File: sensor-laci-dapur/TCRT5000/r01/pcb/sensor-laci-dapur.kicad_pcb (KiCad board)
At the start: 2 copper layers, 66 x 14 mm, 8 parts

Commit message: Sensor Laci Dapur TCRT5000L rev01b
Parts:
- removed Port: Out GND +5, Connectors_Molex:Molex_KK-6410-03_03x2.54mm_Straight
- removed the REF** at (142.2, 95.2)
- removed the REF** at (161.3, 95.2)
- removed Sensor: TCRT5000L, TCRT5000L:XDCR_TCRT5000L
- added M: 1pin, Connect:1pin, F.Cu at (138.2, 97.8)
- added Port1: 1_Out, Connectors_Molex:Molex_KK-6410-03_03x2.54mm_Straight, F.Cu at (177.8, 95.2)
- added REF**: 1pin, Connect:1pin, F.Cu at (164.1, 97.8)
- added Sensor1: TCRT5000L, TCRT5000L:XDCR_TCRT5000L, F.Cu at (151.1, 97.8)
- moved REF** 43.3 mm to (126.5, 97.3)
- moved R1 14.2 mm to (121.9, 105.7), turned to 90 degrees
- moved R2 11.4 mm to (126.5, 105.7), turned to 90 degrees
- moved R3 9.18 mm to (130.8, 105.7), turned to 90 degrees
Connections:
- R1 pad 2: Net-(Port1-Pad2) -> /GND
- R2 pad 1: Net-(Port1-Pad3) -> /Out
- R3 pad 1: Net-(Port1-Pad1) -> /+5V
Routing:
- net Net-(Port1-Pad3): track 62.0 -> 0.00 mm
- net /Out: track 0.00 -> 53.9 mm
- net Net-(Port1-Pad1): track 49.0 -> 0.00 mm
- net Net-(R3-Pad2): track 45.3 -> 27.3 mm
- net Net-(R1-Pad1): track 34.6 -> 42.4 mm
- added copper zone on B.Cu, net /+5V
- added copper zone on F.Cu, net /GND
- removed copper zone on B.Cu, net Net-(Port1-Pad2)
- removed copper zone on F.Cu, net Net-(Port1-Pad2)
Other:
- board size 66 x 14 mm -> 68.6 x 22.9 mm
- net class +5 removed
- net class Default: clearance 0.2 -> 0.3; trace_width 0.25 -> 0.4
- net class Signal added: clearance 0.3, trace_width 0.4, via_dia 0.6, via_drill 0.4
- rule trace_clearance: 0.2 -> 0.3
- board text added: "Out GND +5V"
- board text added: "TCRT500L"
- board text added: "rev01"

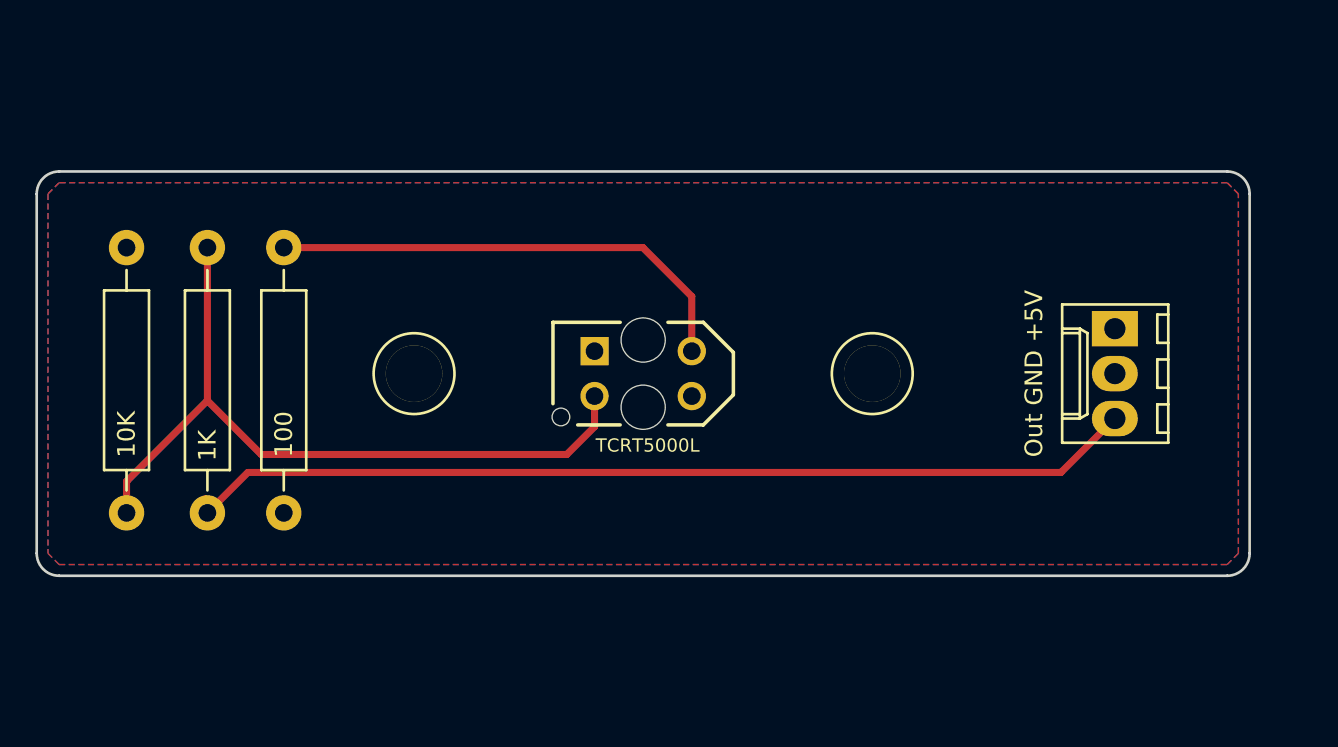
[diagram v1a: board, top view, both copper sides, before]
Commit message: Change connector to JST-XH Angled
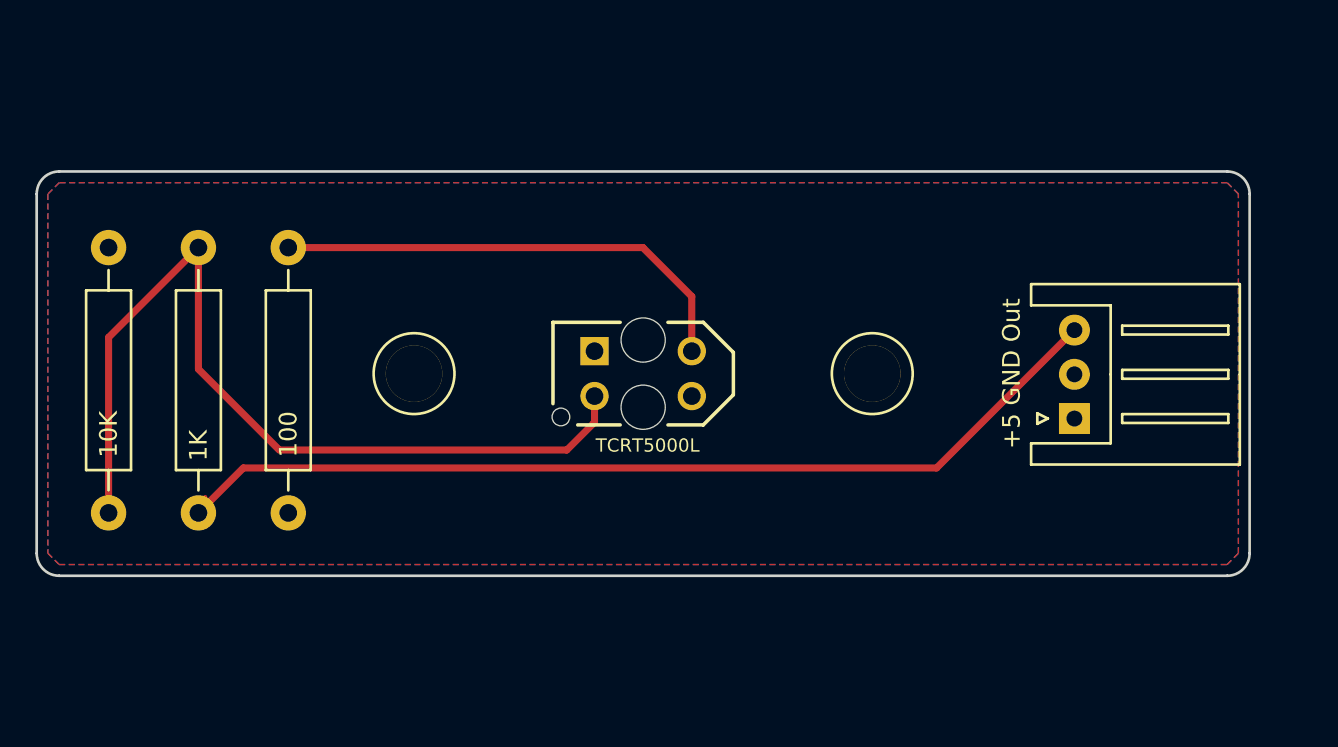
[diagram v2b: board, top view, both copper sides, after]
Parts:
- Port1: footprint Connectors_Molex:Molex_KK-6410-03_03x2.54mm_Straight -> Connectors_JST:JST_XH_S03B-XH-A_03x2.50mm_Angled
- moved Port1 5.57 mm to (175.5, 100.3), turned to 90 degrees
- moved R1 1.02 mm to (120.9, 105.7)
- moved R2 0.51 mm to (126.0, 105.7)
- moved R3 0.25 mm to (131.1, 105.7)
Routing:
- net Net-(R1-Pad1): track 42.4 -> 50.4 mm
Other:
- board text added: "+5 GND Out"
- board text removed: "Out GND +5V"
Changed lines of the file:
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@@
     (40 Dwgs.User user)
     (41 Cmts.User user)
-    (42 Eco1.User user hide)
+    (42 Eco1.User user)
     (43 Eco2.User user)
     (44 Edge.Cuts user)
@@
   )
   (module Resistors_ThroughHole:Resistor_Horizontal_RM15mm (layer F.Cu)
-    (at 126.492 105.664 90)
+    (at 125.984 105.664 90)
     (descr "Resistor, Axial, RM 15mm,")
     (tags "Resistor Axial RM 15mm")
@@
     )
   )
-  (module Connectors_Molex:Molex_KK-6410-03_03x2.54mm_Straight (layer F.Cu)
-    (at 177.8 95.25 270)
-    (descr "Connector Headers with Friction Lock, 22-27-2031, http://www.molex.com/pdm_docs/sd/022272021_sd.pdf")
-    (tags "connector molex kk_6410 22-27-2031")
-    (fp_text reference Port1 (at 1 -4.5 270) (layer F.SilkS) hide
-      (effects (font (size 1 1) (thickness 0.15)))
-    )
-    (fp_text value 1_Out (at 2.54 4.5 270) (layer F.Fab) hide
-      (effects (font (size 1 1) (thickness 0.15)))
-    )
-    (fp_line (start -1.37 -3.02) (end -1.37 2.98) (layer F.SilkS) (width 0.15))
-    (fp_line (start -1.37 2.98) (end 6.45 2.98) (layer F.SilkS) (width 0.15))
-    (fp_line (start 6.45 2.98) (end 6.45 -3.02) (layer F.SilkS) (width 0.15))
-    (fp_line (start 6.45 -3.02) (end -1.37 -3.02) (layer F.SilkS) (width 0.15))
-    (fp_line (start 0 2.98) (end 0 1.98) (layer F.SilkS) (width 0.15))
-    (fp_line (start 0 1.98) (end 5.08 1.98) (layer F.SilkS) (width 0.15))
-    (fp_line (start 5.08 1.98) (end 5.08 2.98) (layer F.SilkS) (width 0.15))
-    (fp_line (start 0 1.98) (end 0.25 1.55) (layer F.SilkS) (width 0.15))
-    (fp_line (start 0.25 1.55) (end 4.83 1.55) (layer F.SilkS) (width 0.15))
-    (fp_line (start 4.83 1.55) (end 5.08 1.98) (layer F.SilkS) (width 0.15))
-    (fp_line (start 0.25 2.98) (end 0.25 1.98) (layer F.SilkS) (width 0.15))
-    (fp_line (start 4.83 2.98) (end 4.83 1.98) (layer F.SilkS) (width 0.15))
-    (fp_line (start -0.8 -3.02) (end -0.8 -2.4) (layer F.SilkS) (width 0.15))
-    (fp_line (start -0.8 -2.4) (end 0.8 -2.4) (layer F.SilkS) (width 0.15))
-    (fp_line (start 0.8 -2.4) (end 0.8 -3.02) (layer F.SilkS) (width 0.15))
-    (fp_line (start 1.74 -3.02) (end 1.74 -2.4) (layer F.SilkS) (width 0.15))
-    (fp_line (start 1.74 -2.4) (end 3.34 -2.4) (layer F.SilkS) (width 0.15))
-    (fp_line (start 3.34 -2.4) (end 3.34 -3.02) (layer F.SilkS) (width 0.15))
-    (fp_line (start 4.28 -3.02) (end 4.28 -2.4) (layer F.SilkS) (width 0.15))
-    (fp_line (start 4.28 -2.4) (end 5.88 -2.4) (layer F.SilkS) (width 0.15))
-    (fp_line (start 5.88 -2.4) (end 5.88 -3.02) (layer F.SilkS) (width 0.15))
-    (fp_line (start -1.9 3.5) (end -1.9 -3.55) (layer F.CrtYd) (width 0.05))
-    (fp_line (start -1.9 -3.55) (end 7 -3.55) (layer F.CrtYd) (width 0.05))
-    (fp_line (start 7 -3.55) (end 7 3.5) (layer F.CrtYd) (width 0.05))
-    (fp_line (start 7 3.5) (end -1.9 3.5) (layer F.CrtYd) (width 0.05))
-    (pad 1 thru_hole rect (at 0 0 270) (size 2 2.6) (drill 1.2) (layers *.Cu *.Mask F.SilkS)
-      (net 3 /+5V))
-    (pad 2 thru_hole oval (at 2.54 0 270) (size 2 2.6) (drill 1.2) (layers *.Cu *.Mask F.SilkS)
-      (net 4 /GND))
-    (pad 3 thru_hole oval (at 5.08 0 270) (size 2 2.6) (drill 1.2) (layers *.Cu *.Mask F.SilkS)
-      (net 5 /Out))
-  )
   (module Resistors_ThroughHole:Resistor_Horizontal_RM15mm (layer F.Cu)
-    (at 121.92 105.664 90)
+    (at 120.904 105.664 90)
     (descr "Resistor, Axial, RM 15mm,")
     (tags "Resistor Axial RM 15mm")
@@
   )
   (module Resistors_ThroughHole:Resistor_Horizontal_RM15mm (layer F.Cu)
-    (at 130.81 105.664 90)
+    (at 131.064 105.664 90)
     (descr "Resistor, Axial, RM 15mm,")
     (tags "Resistor Axial RM 15mm")
@@
     (fp_line (start 0.35052 -0.89916) (end 0.7493 -1.89992) (layer B.SilkS) (width 0.15))
   )
+  (module Connectors_JST:JST_XH_S03B-XH-A_03x2.50mm_Angled (layer F.Cu)
+    (at 175.514 100.33 90)
+    (descr "JST XH series connector, S03B-XH-A, side entry type, through hole")
+    (tags "connector jst xh tht side horizontal angled 2.50mm")
+    (fp_text reference Port1 (at 2.54 -3.81 90) (layer F.SilkS) hide
+      (effects (font (size 1 1) (thickness 0.15)))
+    )
+    (fp_text value 1_Out (at 2.5 10.3 90) (layer F.Fab) hide
+      (effects (font (size 1 1) (thickness 0.15)))
+    )
+    (fp_line (start -2.95 -2.8) (end -2.95 9.7) (layer F.CrtYd) (width 0.05))
+    (fp_line (start -2.95 9.7) (end 7.95 9.7) (layer F.CrtYd) (width 0.05))
+    (fp_line (start 7.95 9.7) (end 7.95 -2.8) (layer F.CrtYd) (width 0.05))
+    (fp_line (start 7.95 -2.8) (end -2.95 -2.8) (layer F.CrtYd) (width 0.05))
+    (fp_line (start 2.5 9.35) (end -2.6 9.35) (layer F.SilkS) (width 0.15))
+    (fp_line (start -2.6 9.35) (end -2.6 -2.45) (layer F.SilkS) (width 0.15))
+    (fp_line (start -2.6 -2.45) (end -1.4 -2.45) (layer F.SilkS) (width 0.15))
+    (fp_line (start -1.4 -2.45) (end -1.4 2.05) (layer F.SilkS) (width 0.15))
+    (fp_line (start -1.4 2.05) (end 2.5 2.05) (layer F.SilkS) (width 0.15))
+    (fp_line (start 2.5 9.35) (end 7.6 9.35) (layer F.SilkS) (width 0.15))
+    (fp_line (start 7.6 9.35) (end 7.6 -2.45) (layer F.SilkS) (width 0.15))
+    (fp_line (start 7.6 -2.45) (end 6.4 -2.45) (layer F.SilkS) (width 0.15))
+    (fp_line (start 6.4 -2.45) (end 6.4 2.05) (layer F.SilkS) (width 0.15))
+    (fp_line (start 6.4 2.05) (end 2.5 2.05) (layer F.SilkS) (width 0.15))
+    (fp_line (start -0.25 2.7) (end -0.25 8.7) (layer F.SilkS) (width 0.15))
+    (fp_line (start -0.25 8.7) (end 0.25 8.7) (layer F.SilkS) (width 0.15))
+    (fp_line (start 0.25 8.7) (end 0.25 2.7) (layer F.SilkS) (width 0.15))
+    (fp_line (start 0.25 2.7) (end -0.25 2.7) (layer F.SilkS) (width 0.15))
+    (fp_line (start 2.25 2.7) (end 2.25 8.7) (layer F.SilkS) (width 0.15))
+    (fp_line (start 2.25 8.7) (end 2.75 8.7) (layer F.SilkS) (width 0.15))
+    (fp_line (start 2.75 8.7) (end 2.75 2.7) (layer F.SilkS) (width 0.15))
+    (fp_line (start 2.75 2.7) (end 2.25 2.7) (layer F.SilkS) (width 0.15))
+    (fp_line (start 4.75 2.7) (end 4.75 8.7) (layer F.SilkS) (width 0.15))
+    (fp_line (start 4.75 8.7) (end 5.25 8.7) (layer F.SilkS) (width 0.15))
+    (fp_line (start 5.25 8.7) (end 5.25 2.7) (layer F.SilkS) (width 0.15))
+    (fp_line (start 5.25 2.7) (end 4.75 2.7) (layer F.SilkS) (width 0.15))
+    (fp_line (start 0 -1.5) (end -0.3 -2.1) (layer F.SilkS) (width 0.15))
+    (fp_line (start -0.3 -2.1) (end 0.3 -2.1) (layer F.SilkS) (width 0.15))
+    (fp_line (start 0.3 -2.1) (end 0 -1.5) (layer F.SilkS) (width 0.15))
+    (pad 1 thru_hole rect (at 0 0 90) (size 1.75 1.75) (drill 0.9) (layers *.Cu *.Mask F.SilkS)
+      (net 3 /+5V))
+    (pad 2 thru_hole circle (at 2.5 0 90) (size 1.75 1.75) (drill 0.9) (layers *.Cu *.Mask F.SilkS)
+      (net 4 /GND))
+    (pad 3 thru_hole circle (at 5 0 90) (size 1.75 1.75) (drill 0.9) (layers *.Cu *.Mask F.SilkS)
+      (net 5 /Out))
+    (model Connectors_JST.3dshapes/JST_XH_S03B-XH-A_03x2.50mm_Angled.wrl
+      (at (xyz 0 0 0))
+      (scale (xyz 1 1 1))
+      (rotate (xyz 0 0 0))
+    )
+  )
   (gr_text TCRT500L (at 183.896 91.694) (layer B.SilkS)
     (effects (font (size 1.5 1.5) (thickness 0.3)) (justify left mirror))
@@
     (effects (font (size 1 1) (thickness 0.2)) (justify left mirror))
   )
-  (gr_text "Out GND +5V" (at 173.228 97.79 90) (layer F.SilkS)
+  (gr_text "+5 GND Out" (at 171.958 97.79 90) (layer F.SilkS)
     (effects (font (size 1 1) (thickness 0.15)))
   )
@@
   (gr_line (start 118.11 109.22) (end 184.15 109.22) (angle 90) (layer Edge.Cuts) (width 0.15))
   (gr_line (start 116.84 87.63) (end 116.84 107.95) (angle 90) (layer Edge.Cuts) (width 0.15))
-  (segment (start 121.92 105.664) (end 121.92 103.886) (width 0.4) (layer F.Cu) (net 1))
-  (segment (start 121.92 103.886) (end 126.492 99.314) (width 0.4) (layer F.Cu) (net 1))
-  (segment (start 126.492 90.664) (end 126.492 99.314) (width 0.4) (layer F.Cu) (net 1))
-  (segment (start 148.38 100.794) (end 148.38 99.06) (width 0.4) (layer F.Cu) (net 1))
-  (segment (start 146.812 102.362) (end 148.38 100.794) (width 0.4) (layer F.Cu) (net 1))
-  (segment (start 129.54 102.362) (end 146.812 102.362) (width 0.4) (layer F.Cu) (net 1))
-  (segment (start 126.492 99.314) (end 129.54 102.362) (width 0.4) (layer F.Cu) (net 1))
-  (segment (start 130.81 90.664) (end 151.116 90.664) (width 0.4) (layer F.Cu) (net 2))
+  (segment (start 125.984 97.536) (end 125.984 90.664) (width 0.4) (layer F.Cu) (net 1))
+  (segment (start 130.556 102.108) (end 125.984 97.536) (width 0.4) (layer F.Cu) (net 1))
+  (segment (start 146.812 102.108) (end 130.556 102.108) (width 0.4) (layer F.Cu) (net 1))
+  (segment (start 148.38 100.54) (end 146.812 102.108) (width 0.4) (layer F.Cu) (net 1))
+  (segment (start 148.38 99.06) (end 148.38 100.54) (width 0.4) (layer F.Cu) (net 1))
+  (segment (start 120.904 95.744) (end 125.984 90.664) (width 0.4) (layer F.Cu) (net 1))
+  (segment (start 120.904 105.664) (end 120.904 95.744) (width 0.4) (layer F.Cu) (net 1))
   (segment (start 153.88 93.428) (end 153.88 96.52) (width 0.4) (layer F.Cu) (net 2))
   (segment (start 151.116 90.664) (end 153.88 93.428) (width 0.4) (layer F.Cu) (net 2))
+  (segment (start 131.064 90.664) (end 151.116 90.664) (width 0.4) (layer F.Cu) (net 2))
   (segment (start 130.81 90.664) (end 130.81 90.678) (width 0.4) (layer F.Cu) (net 2))
-  (segment (start 126.492 105.664) (end 128.778 103.378) (width 0.4) (layer F.Cu) (net 5))
-  (segment (start 174.752 103.378) (end 177.8 100.33) (width 0.4) (layer F.Cu) (net 5))
-  (segment (start 128.778 103.378) (end 174.752 103.378) (width 0.4) (layer F.Cu) (net 5))
+  (segment (start 167.72 103.124) (end 175.514 95.33) (width 0.4) (layer F.Cu) (net 5))
+  (segment (start 128.524 103.124) (end 167.72 103.124) (width 0.4) (layer F.Cu) (net 5))
+  (segment (start 125.984 105.664) (end 128.524 103.124) (width 0.4) (layer F.Cu) (net 5))
   (segment (start 126.365 105.17) (end 126.365 104.775) (width 0.25) (layer F.Cu) (net 5))
   (zone (net 4) (net_name /GND) (layer F.Cu) (hatch edge 0.508)

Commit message: Adjust pin order and component locations
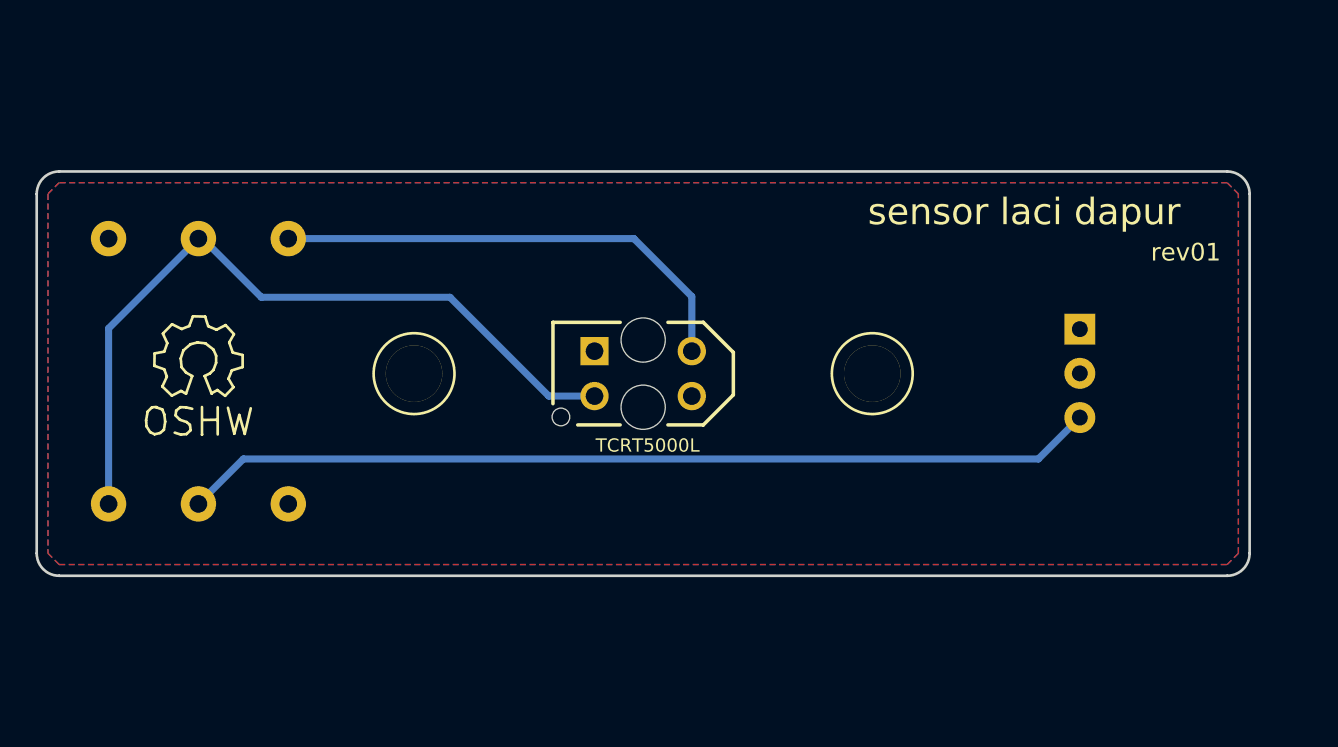
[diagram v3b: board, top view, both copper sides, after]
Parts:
- removed Port1: 1_Out, Connectors_JST:JST_XH_S03B-XH-A_03x2.50mm_Angled
- added U1: 1_Out, Connectors_JST:JST_XH_S03B-XH-A_03x2.50mm_Angled, B.Cu at (175.8, 95.3)
- R1, R2, R3: moved to B.Cu
- REF**: moved to F.Cu
- moved REF** 0.57 mm to (126.0, 97.0), turned to 0 degrees
- moved R1 0.51 mm to (120.9, 105.2)
- moved R2 0.51 mm to (126.0, 105.2)
- moved R3 0.51 mm to (131.1, 105.2)
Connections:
- R1 pad 2: /GND -> /+5V
- R3 pad 1: /+5V -> /GND
- Sensor1 pad 1: /+5V -> /GND
- Sensor1 pad 3: /GND -> /+5V
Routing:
- net Net-(R1-Pad1): track 50.4 -> 43.2 mm
- net /Out: track 54.2 -> 52.3 mm
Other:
- board text added: "GND +5 Out"
- board text removed: "+5 GND Out"
- board text removed: "TCRT500L"

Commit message: Add SMD resistor pad to the sensor board
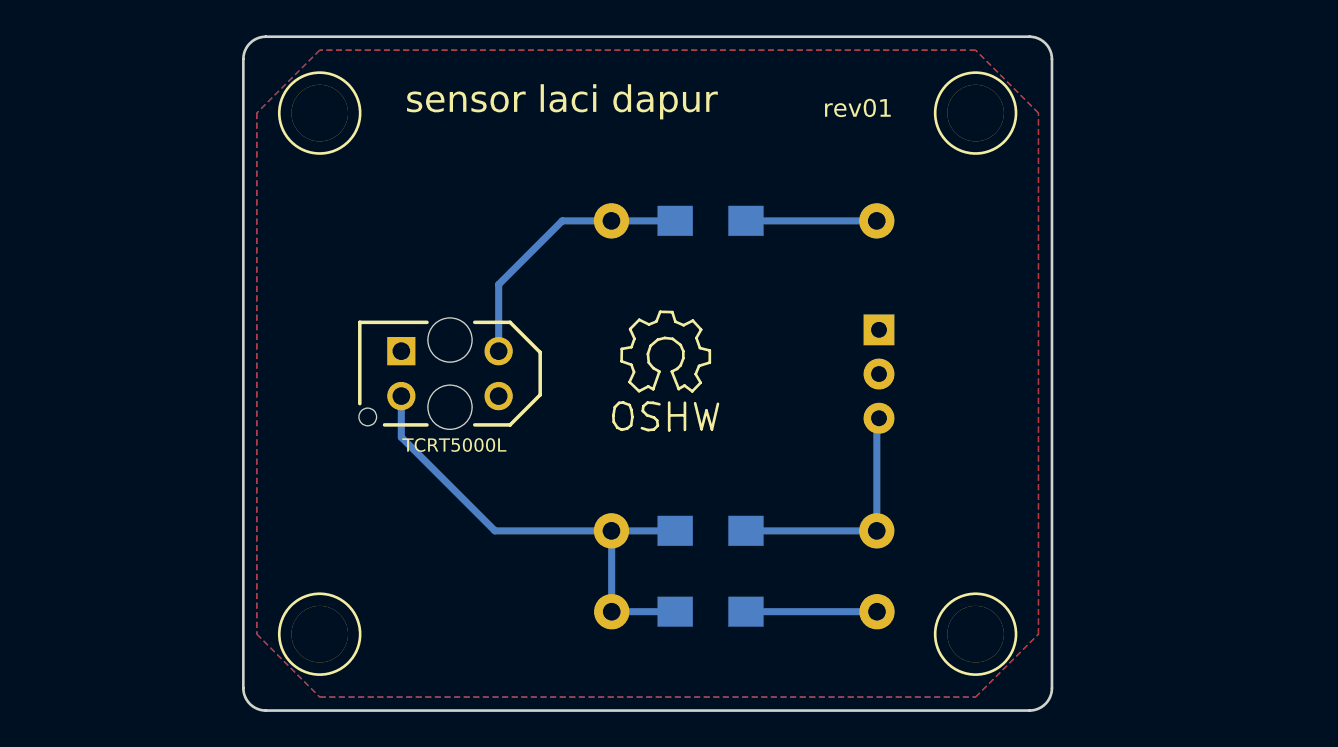
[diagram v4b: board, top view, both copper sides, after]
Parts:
- added R100: R_1206_HandSoldering, Resistors_SMD:R_1206_HandSoldering, B.Cu at (154.9, 89.2)
- added R10K: R_1206_HandSoldering, Resistors_SMD:R_1206_HandSoldering, B.Cu at (154.9, 111.3)
- added R1K: R_1206_HandSoldering, Resistors_SMD:R_1206_HandSoldering, B.Cu at (154.9, 106.7)
- added REF**: 1pin, Connect:1pin, F.Cu at (132.8, 112.5)
- added REF**: 1pin, Connect:1pin, F.Cu at (169.9, 112.5)
- moved R2 38.4 mm to (164.3, 106.7), turned to 180 degrees
- moved R3 36.9 mm to (164.3, 89.2), turned to 180 degrees
- moved R1 29.1 mm to (149.4, 111.3), turned to 0 degrees
- moved REF** 26.4 mm to (152.4, 96.8)
- moved REF** 15.8 mm to (169.9, 83.1)
- moved M 15.7 mm to (132.8, 83.1)
- moved U1 11.4 mm to (164.5, 95.3)
- moved Sensor1 10.9 mm to (140.2, 97.8)
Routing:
- net /Out: track 52.3 -> 13.8 mm
- net Net-(R1-Pad1): track 43.2 -> 28.2 mm
- net Net-(R3-Pad2): track 27.3 -> 15.2 mm
- net /+5V: track 0.00 -> 7.43 mm
- net (no net): track 0.00 -> 7.40 mm
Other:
- board size 68.6 x 22.9 mm -> 45.7 x 38.1 mm
